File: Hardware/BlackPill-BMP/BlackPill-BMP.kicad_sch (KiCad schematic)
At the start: 33 parts, among them J1 JTAG, J2 VCC, J3 GND, J4 SWO, J5 GDB_COMM, J6 TVCC, J7 LogicAna, J8 Conn_01x10, J9 Conn_01x11, U1 BlueAndBlackPill, U2 AD8531ARTZ, U3 TXB0108EPW, U4 TXBN0304RUT

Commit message: Updated Blue-Black-Pill prototype board.
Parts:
- added C9: 100nF, Capacitor_SMD:C_0603_1608Metric_Pad1.08x0.95mm_HandSolder, symbol Device:C
- added D1: 82356050050, Diode_SMD:D_0603_1608Metric_Pad1.05x0.95mm_HandSolder, symbol Device:D_TVS
- added J9: Conn_01x05_Male, Connector_PinHeader_2.54mm:PinHeader_1x05_P2.54mm_Vertical, symbol Connector:Conn_01x05_Male
- added U3: SN74LVC1G125, Package_TO_SOT_SMD:SOT-23-5, symbol 74LVC1G125SE-7:SN74LVC1G125
- J10: renamed from J9; value Conn_01x11 -> Conn_01x12_Male; symbol Connector_Generic:Conn_01x12 -> Connector:Conn_01x12_Male
- J8: value Conn_01x10 -> Conn_01x06_Male; footprint Connector_PinHeader_2.54mm:PinHeader_1x10_P2.54mm_Vertical -> Connector_PinHeader_2.54mm:PinHeader_1x06_P2.54mm_Vertical; symbol Connector_Generic:Conn_01x10 -> Connector:Conn_01x06_Male
- renumbered C9 to C10, C10 to C11, C11 to C12, C12 to C13, D1 to D2, R6 to R5, R7 to R6, U3 to U4, U4 to U5
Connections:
- net PB12 is gone; now on net JENA: J8.1 (Pin_1), U1.A1 (PB12), U1.B1 (PB12)
- net TVCC is gone; now on net VCC: C10.2, C11.2, C6.2, C7.2, C8.2, F1.2, J1.2 (Pin_2), J6.1 (Pin_1), J6.2 (Pin_2), U2.4 (-), U4.1 (VCCA), U5.1 (VCCA)
- net +3V3: now also C9.2, U3.5 (VCC); no longer R5.2
- net GND: now also D2.1 (K), C9.1, D1.1 (A1), U3.3 (GND); no longer J8.10 (Pin_10)
- net JENA: no longer J8.5 (Pin_5), U1.A6 (PA9), U1.B6 (PA9)
- net PB0: now also J10.3 (Pin_3); no longer J10.10 (Pin_10)
- net PB1: now also J10.2 (Pin_2); no longer J10.11 (Pin_11)
- net PB4: now also J9.2 (Pin_2); no longer J8.7 (Pin_7)
- net PB5: now also J9.3 (Pin_3); no longer J8.8 (Pin_8)
- net TV_PWM: now also J9.4 (Pin_4); no longer J8.9 (Pin_9)
- net VREF_2: now also J10.11 (Pin_11), D1.2 (A2); no longer J10.2 (Pin_2)
- net mRST: now also J10.10 (Pin_10); no longer J10.3 (Pin_3)
- net mRXD: now also J10.8 (Pin_8); no longer J10.5 (Pin_5)
- net mTCK: now also J10.1 (Pin_1), J10.6 (Pin_6), J8.5 (Pin_5); no longer J10.12 (Pin_12), J10.7 (Pin_7), J8.4 (Pin_4)
- net mTDI: now also J10.4 (Pin_4); no longer J10.9 (Pin_9)
- net mTDO: now also J10.5 (Pin_5), U3.4 (Y); no longer J10.8 (Pin_8), U1.A4 (PB15), U1.B4 (PB15)
- net mTEST: now also J10.7 (Pin_7); no longer J10.6 (Pin_6)
- net mTMS: now also J9.1 (Pin_1); no longer J8.6 (Pin_6)
- net mTXD: now also J10.9 (Pin_9); no longer J10.4 (Pin_4)
- net VCC: now reaches J5.4 (Pin_4)
- net LEDG renamed PB9
- net PB9: now also J9.5 (Pin_5); no longer D2.1 (K)
- net PC13 renamed LEDS
- net LEDS: now also J10.12 (Pin_12), R5.2; no longer J10.1 (Pin_1)
- new net SBWO: J8.4 (Pin_4), U1.A4 (PB15), U1.B4 (PB15), U3.2 (A)
- new net SBW_DIR: J8.6 (Pin_6), U1.A6 (PA9), U1.B6 (PA9), U3.1 (~{OE})
- no-connect marks 21 -> 20
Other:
- note added: "(NM)"
- note added: "USART1: GDB Port TRACESWO: External debugger SPI1: JTAG interface (SPI and bit-bang) SPI2: SBW interface (SPI and bit-bang) TIM1: JTMS signal generation GPIO: LEDG, JTAG (partial) Rev2: Swap LRXD and LTXD; Swap nTMS and JENA; Redesign of the ESD protection ICs Changed from TXS0108 to TXB0304. Using integrated ESD protection. Added SBW Direction buffer"
- note removed: "USART1: GDB Port TRACESWO: External debugger SPI1: JTAG interface (SPI and bit-bang) SPI2: SBW interface (SPI and bit-bang) TIM1: JTMS signal generation GPIO: LEDG, JTAG (partial) Rev2: Swap LRXD and LTXD; Swap nTMS and JENA; Redesign of the ESD protection ICs Changed from TXS0108 to TXB0304. Using integrated ESD protection."
- moved on the sheet: C5, C7, C8, D2, J1, J3, J4, J5, J6, J7, R3, R4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

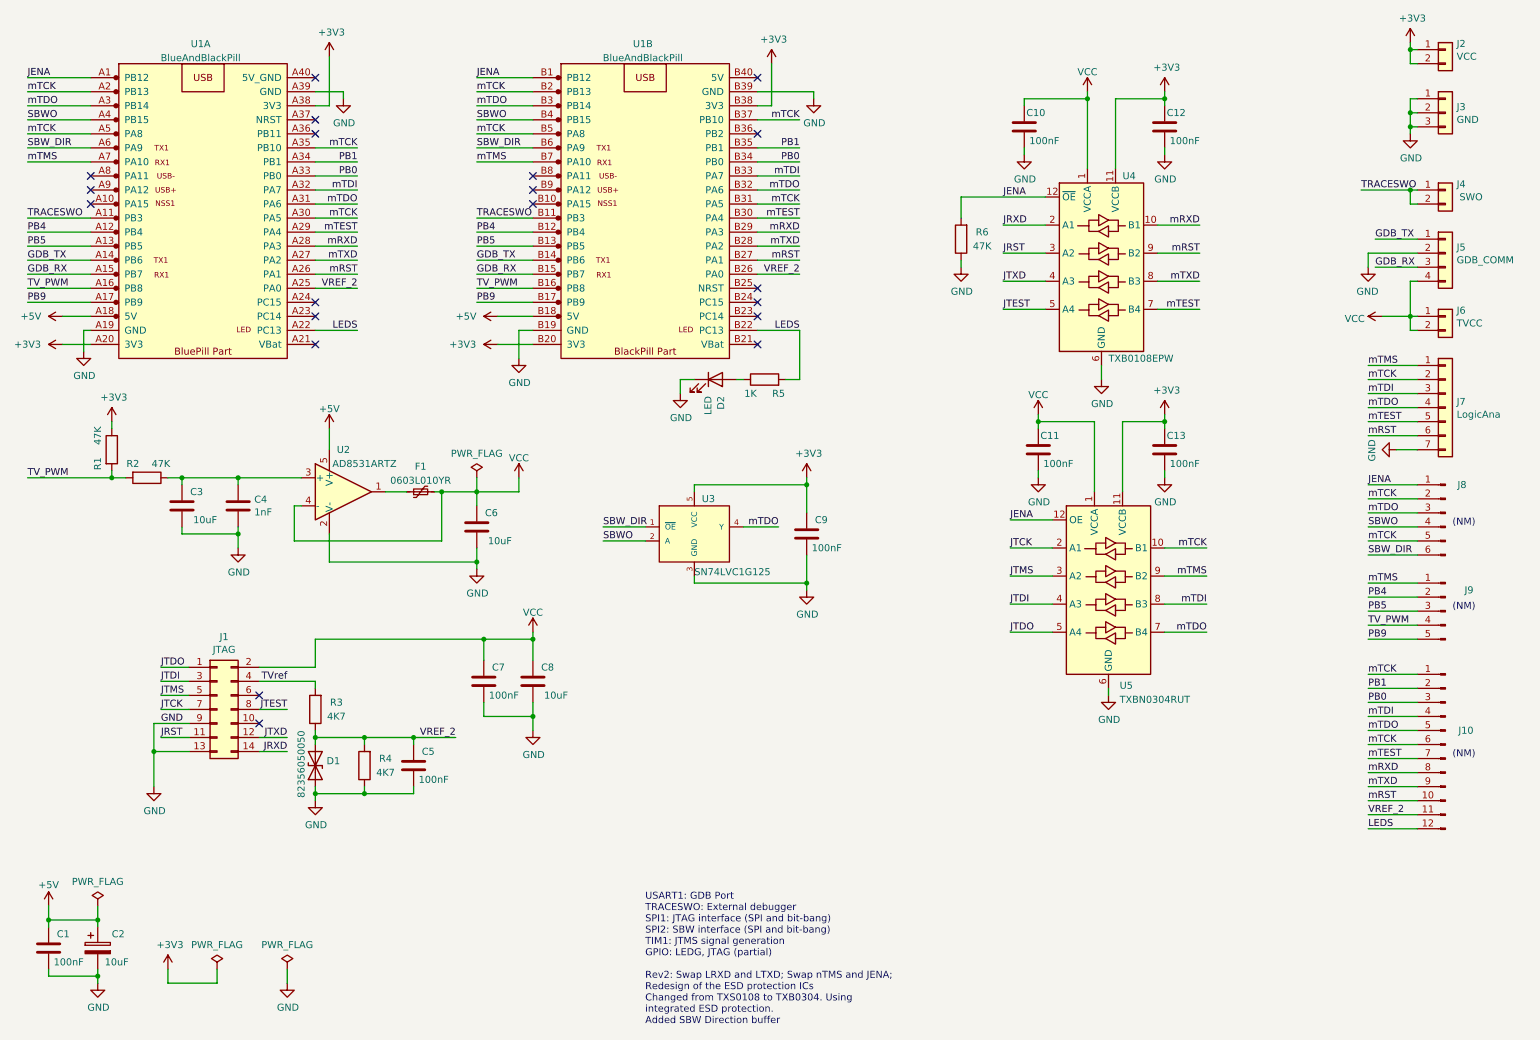
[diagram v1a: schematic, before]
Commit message: Complete review of output stage of Proto board
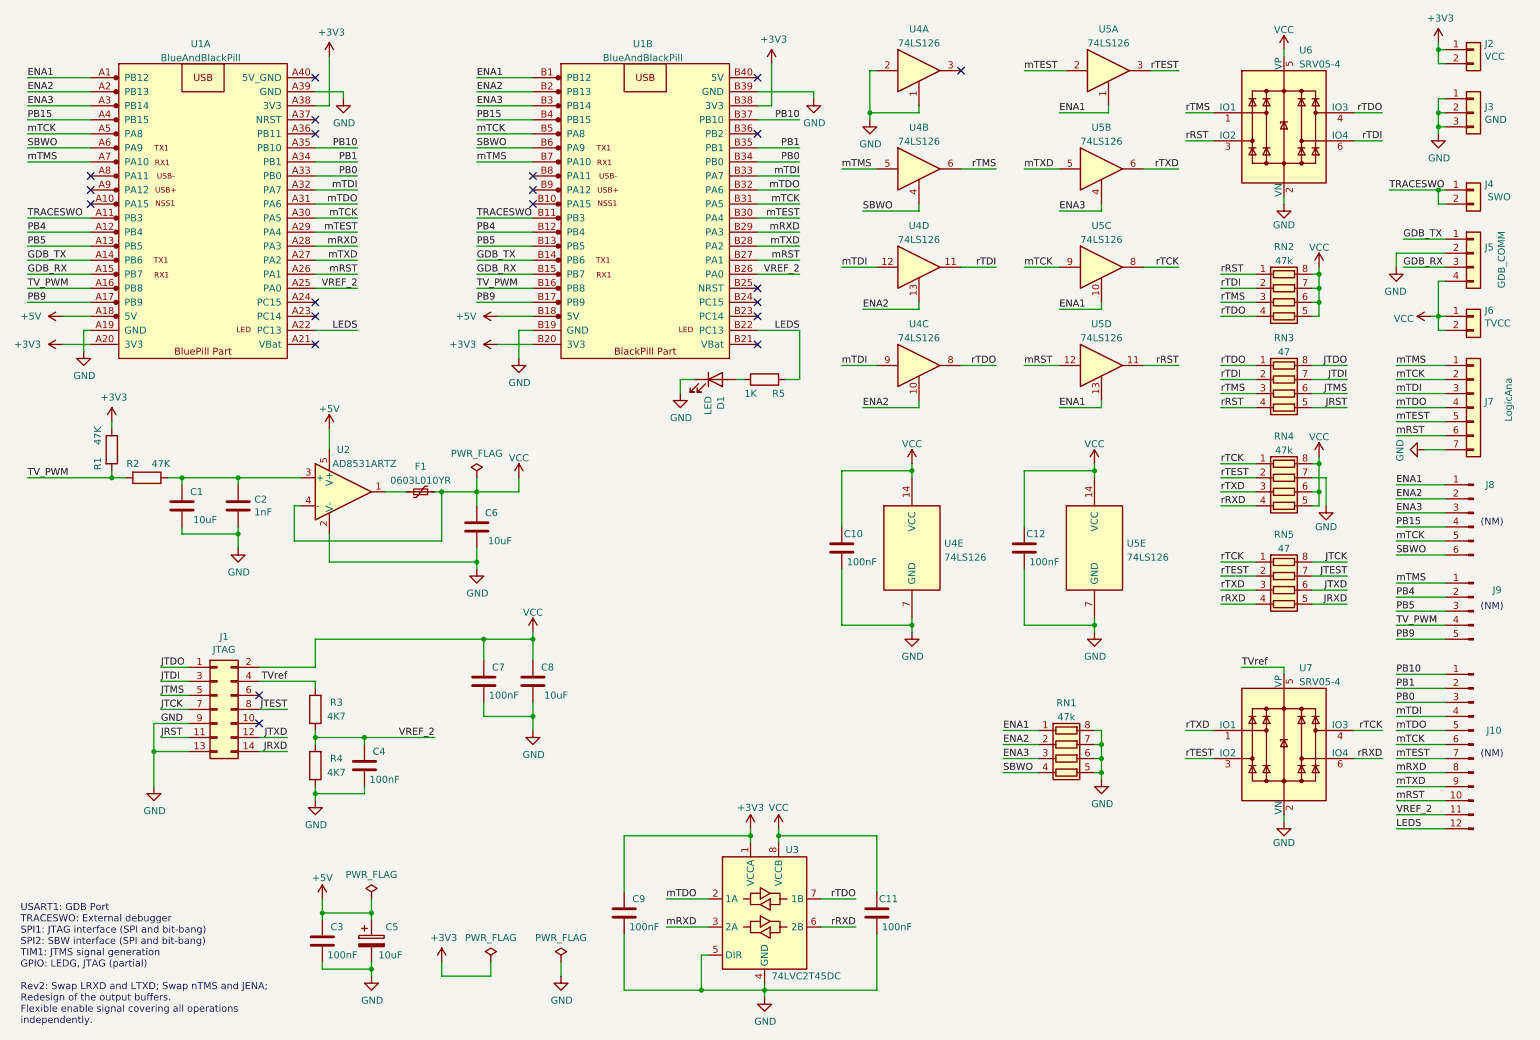
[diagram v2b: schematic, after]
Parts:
- removed C13: 100nF, Capacitor_SMD:C_0603_1608Metric_Pad1.08x0.95mm_HandSolder, symbol Device:C
- removed D1: 82356050050, Diode_SMD:D_0603_1608Metric_Pad1.05x0.95mm_HandSolder, symbol Device:D_TVS
- removed R6: 47K, Resistor_SMD:R_0603_1608Metric_Pad0.98x0.95mm_HandSolder, symbol Device:R
- removed U3: SN74LVC1G125, Package_TO_SOT_SMD:SOT-23-5, symbol 74LVC1G125SE-7:SN74LVC1G125
- removed U4: TXB0108EPW, Package_DFN_QFN:Texas_R_PUQFN-N12, symbol Logic_LevelTranslator:TXBN0304RUT
- removed U5: TXBN0304RUT, Package_DFN_QFN:Texas_R_PUQFN-N12, symbol Logic_LevelTranslator:TXB0304RUT
- added RN1, RN2, RN4: 47k, Resistor_SMD:R_Array_Convex_4x0402, symbol Device:R_Pack04
- added RN3, RN5: 47, Resistor_SMD:R_Array_Convex_4x0402, symbol Device:R_Pack04
- added U3: 74LVC2T45DC, Package_SO:VSSOP-8_2.3x2mm_P0.5mm, symbol Logic_LevelTranslator:74LVC2T45DC
- added U4, U5: 74LS126, Package_SO:TSSOP-14_4.4x5mm_P0.65mm, symbol 74xx:74LS126
- added U6, U7: SRV05-4, Package_TO_SOT_SMD:SOT-23-6, symbol Power_Protection:SRV05-4
- renumbered C3 to C1, C11 to C10, C10 to C11, C9 to C12, C4 to C2, C1 to C3, C5 to C4, C2 to C5, C12 to C9, D2 to D1
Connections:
- net SBW_DIR is gone; now on net SBWO: J8.6 (Pin_6), U1.A6 (PA9), U1.B6 (PA9)
- net +3V3: now also U3.1 (VCCA); no longer C12.2
- net GND: now also RN1.5 (R4.2), RN1.6 (R3.2), RN1.7 (R2.2), RN1.8 (R1.2), RN4.7 (R2.2), U3.4 (GND), U3.5 (DIR), U4.1, U4.2, U4.7 (GND), U5.7 (GND), U6.2 (VN), U7.2 (VN)
- net JRST: now also RN3.5 (R4.2)
- net JRXD: now also RN5.5 (R4.2)
- net JTCK: now also RN5.8 (R1.2)
- net JTDI: now also RN3.7 (R2.2)
- net JTDO: now also RN3.8 (R1.2)
- net JTEST: now also RN5.7 (R2.2)
- net JTMS: now also RN3.6 (R3.2)
- net JTXD: now also RN5.6 (R3.2)
- net SBWO: now also RN1.4 (R4.1), U4.4; no longer J8.4 (Pin_4), U1.A4 (PB15), U1.B4 (PB15)
- net TVref: now also U7.5 (VP)
- net VCC: now also C12.2, RN2.5 (R4.2), RN2.6 (R3.2), RN2.7 (R2.2), RN2.8 (R1.2), RN4.5 (R4.2), RN4.6 (R3.2), RN4.8 (R1.2), U3.8 (VCCB), U4.14 (VCC), U5.14 (VCC), U6.5 (VP)
- net mRST: now also U5.12
- net mRXD: now also U3.3 (2A)
- net mTCK: now also U5.9; no longer J10.1 (Pin_1), J8.2 (Pin_2), U1.A2 (PB13), U1.A35 (PB10), U1.B2 (PB13), U1.B37 (PB10)
- net mTDI: now also U4.12, U4.9
- net mTDO: now also U3.2 (1A); no longer J8.3 (Pin_3), U1.A3 (PB14), U1.B3 (PB14)
- net mTEST: now also U5.2
- net mTMS: now also U4.5
- net mTXD: now also U5.5
- net JENA renamed ENA1
- net ENA1: now also RN1.1 (R1.1), U5.1, U5.10, U5.13
- new net ENA2: J8.2 (Pin_2), RN1.2 (R2.1), U1.A2 (PB13), U1.B2 (PB13), U4.10, U4.13
- new net ENA3: J8.3 (Pin_3), RN1.3 (R3.1), U1.A3 (PB14), U1.B3 (PB14), U5.4
- new net PB10: J10.1 (Pin_1), U1.A35 (PB10), U1.B37 (PB10)
- new net PB15: J8.4 (Pin_4), U1.A4 (PB15), U1.B4 (PB15)
- new net rRST: RN2.1 (R1.1), RN3.4 (R4.1), U5.11, U6.3 (IO2)
- new net rRXD: RN4.4 (R4.1), RN5.4 (R4.1), U3.6 (2B), U7.6 (IO4)
- new net rTCK: RN4.1 (R1.1), RN5.1 (R1.1), U5.8, U7.4 (IO3)
- new net rTDI: RN2.2 (R2.1), RN3.2 (R2.1), U4.11, U6.6 (IO4)
- new net rTDO: RN2.4 (R4.1), RN3.1 (R1.1), U3.7 (1B), U4.8, U6.4 (IO3)
- new net rTEST: RN4.2 (R2.1), RN5.2 (R2.1), U5.3, U7.3 (IO2)
- new net rTMS: RN2.3 (R3.1), RN3.3 (R3.1), U4.6, U6.1 (IO1)
- new net rTXD: RN4.3 (R3.1), RN5.3 (R3.1), U5.6, U7.1 (IO1)
- no-connect marks 20 -> 21
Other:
- note added: "USART1: GDB Port TRACESWO: External debugger SPI1: JTAG interface (SPI and bit-bang) SPI2: SBW interface (SPI and bit-bang) TIM1: JTMS signal generation GPIO: LEDG, JTAG (partial) Rev2: Swap LRXD and LTXD; Swap nTMS and JENA; Redesign of the output buffers. Flexible enable signal covering all operations independently."
- note removed: "USART1: GDB Port TRACESWO: External debugger SPI1: JTAG interface (SPI and bit-bang) SPI2: SBW interface (SPI and bit-bang) TIM1: JTMS signal generation GPIO: LEDG, JTAG (partial) Rev2: Swap LRXD and LTXD; Swap nTMS and JENA; Redesign of the ESD protection ICs Changed from TXS0108 to TXB0304. Using integrated ESD protection. Added SBW Direction buffer"
- moved on the sheet: C10, C11, C12, C3, C4, C5, C9, J10, J2, J3, J4, J5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

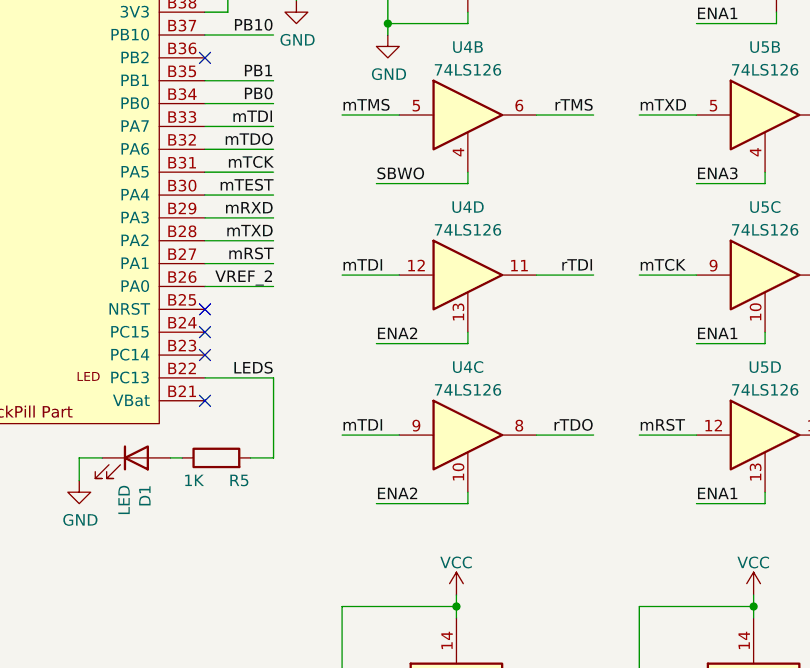
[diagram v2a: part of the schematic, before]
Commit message: Fixed an error on the TDI/TDO line selection
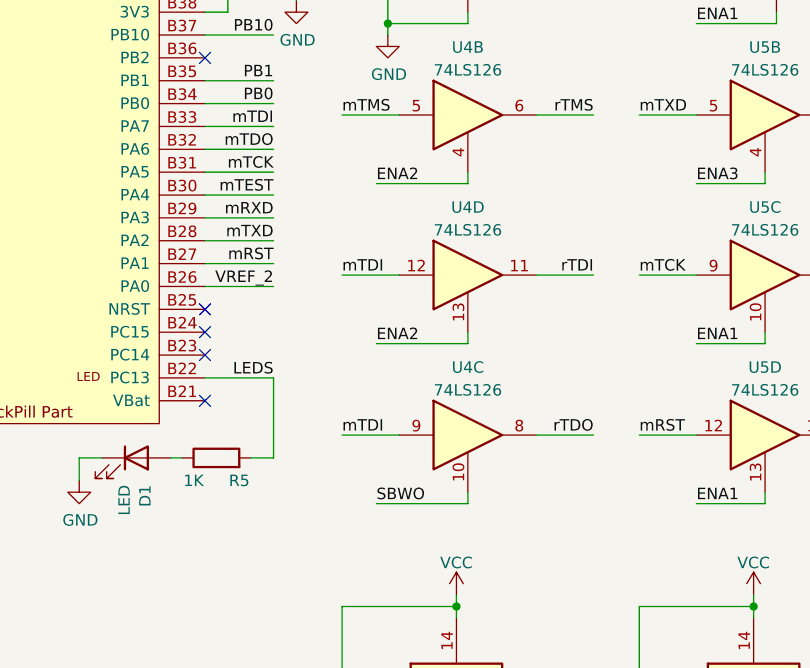
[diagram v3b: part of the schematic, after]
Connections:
- net ENA2: now also U4.4; no longer U4.10
- net SBWO: now also U4.10; no longer U4.4
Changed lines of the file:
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@@
     (effects (font (size 1.27 1.27)) (justify left bottom))
   )
-  (label "SBWO" (at 166.37 49.53 0)
+  (label "SBWO" (at 166.37 85.09 0)
     (effects (font (size 1.27 1.27)) (justify left bottom))
   )
@@
     (effects (font (size 1.27 1.27)) (justify left bottom))
   )
-  (label "ENA2" (at 166.37 85.09 0)
+  (label "ENA2" (at 166.37 49.53 0)
     (effects (font (size 1.27 1.27)) (justify left bottom))
   )

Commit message: - Components review
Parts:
- RN3, RN5: value 47 -> 100
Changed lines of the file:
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@@
   (title_block
     (title "MSPBMP Development Protoboard")
-    (date "2022-11-17")
+    (date "2022-11-27")
     (rev "2")
     (company "Mathias Gruber")
@@
     (in_bom yes) (on_board yes) (fields_autoplaced)
     (property "Reference" "RN3" (id 0) (at 242.57 72.5002 90))
-    (property "Value" "47" (id 1) (at 242.57 75.0371 90))
+    (property "Value" "100" (id 1) (at 242.57 75.0371 90))
     (property "Footprint" "Resistor_SMD:R_Array_Convex_4x0402" (id 2) (at 242.57 89.535 90)
       (effects (font (size 1.27 1.27)) hide)
@@
     (in_bom yes) (on_board yes) (fields_autoplaced)
     (property "Reference" "RN5" (id 0) (at 242.57 108.0602 90))
-    (property "Value" "47" (id 1) (at 242.57 110.5971 90))
+    (property "Value" "100" (id 1) (at 242.57 110.5971 90))
     (property "Footprint" "Resistor_SMD:R_Array_Convex_4x0402" (id 2) (at 242.57 125.095 90)
       (effects (font (size 1.27 1.27)) hide)
@@
     )
     (path "/306ecf0c-46bf-49c8-ba74-cd8844253fcd"
-      (reference "RN3") (unit 1) (value "47") (footprint "Resistor_SMD:R_Array_Convex_4x0402")
+      (reference "RN3") (unit 1) (value "100") (footprint "Resistor_SMD:R_Array_Convex_4x0402")
     )
     (path "/45515b1d-6d7a-49f0-b27f-d513b73767ce"
@@
     )
     (path "/689c2322-e8bb-4905-ab36-cd320491bde0"
-      (reference "RN5") (unit 1) (value "47") (footprint "Resistor_SMD:R_Array_Convex_4x0402")
+      (reference "RN5") (unit 1) (value "100") (footprint "Resistor_SMD:R_Array_Convex_4x0402")
     )
     (path "/b141b0b5-1c34-438f-8f5a-a2e1dda2ee83"
